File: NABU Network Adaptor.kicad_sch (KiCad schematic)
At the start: 20 parts, among them J2 PC, J3 RF Module, J5 LEDs, U1 SN74LS164N, U10 UA9638CP, U11 UA9637ATC, U13 SN74LS164N, U19 LM339N, U20 SN74LS164N, U21 SN74LS86N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

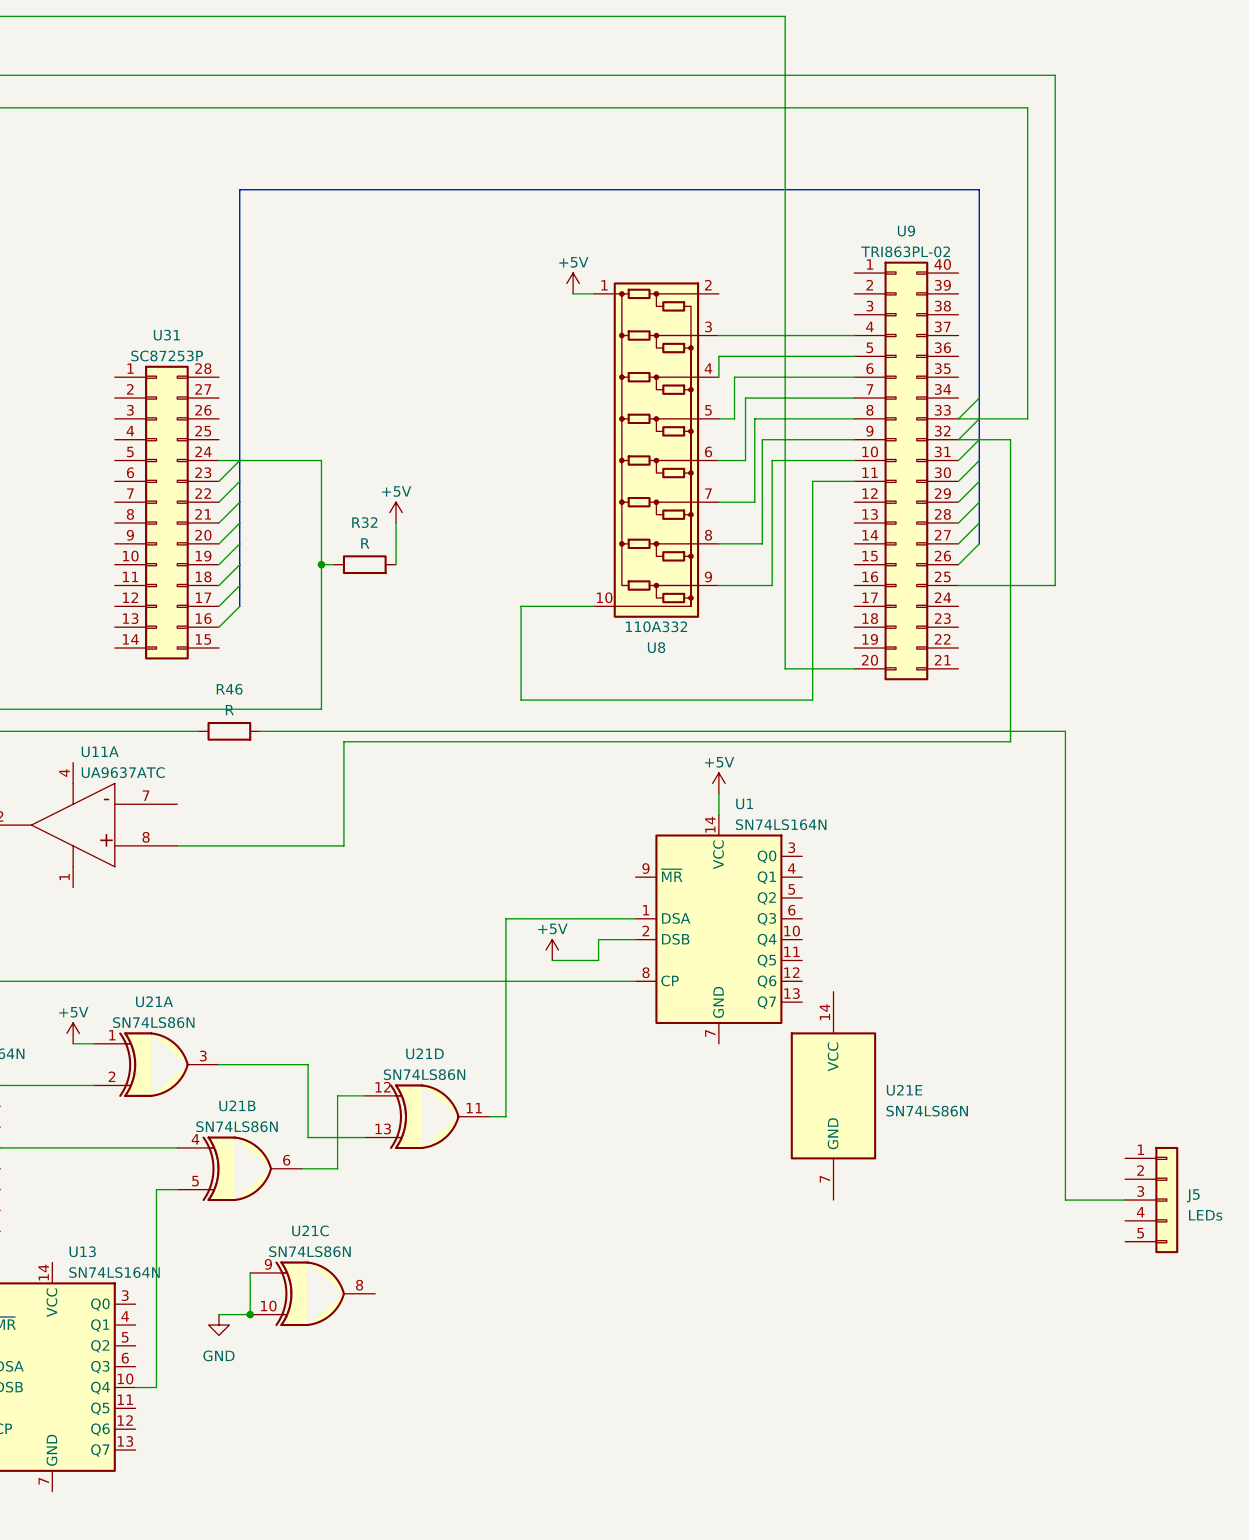
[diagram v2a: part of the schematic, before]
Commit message: Add LED wiring
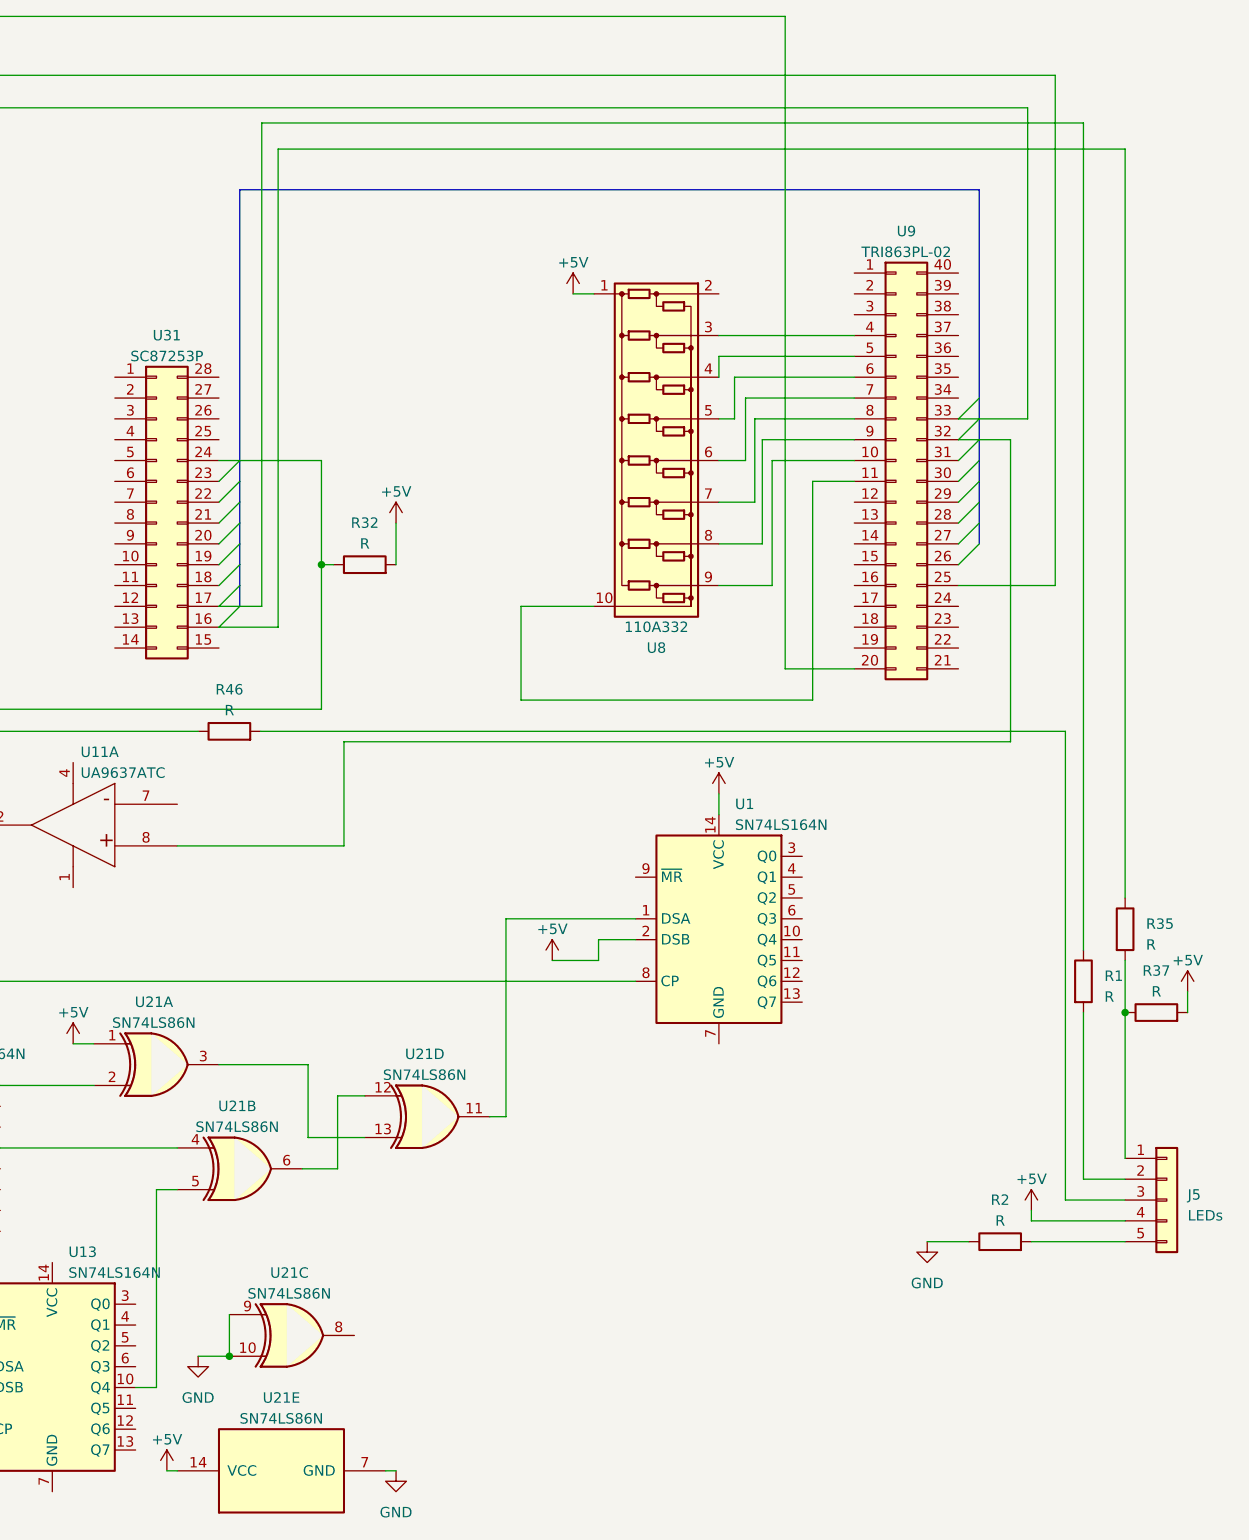
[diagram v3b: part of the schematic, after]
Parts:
- added R1, R2, R35, R37: R, symbol Device:R
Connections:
- net +5V: now also J5.4 (Pin_4), U21.14 (VCC), R37.2
- net GND: now also U21.7 (GND), R2.1
- net at J5.1 (Pin_1): now also R35.2, R37.1
- net at J5.2 (Pin_2): now also R1.2
- net at J5.5 (Pin_5): now also R2.2
- net at U31.16 (Pin_16): now also R35.1
- net at U31.17 (Pin_17): now also R1.1
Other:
- moved on the sheet: U21C, U21E

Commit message: More info on the 74164s
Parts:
- added C1, C12, C13, C20, CB1: C, symbol Device:C
- added U12: SN74LS164N, symbol 74xx:74HCT164
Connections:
- net +5V: now also U13.14 (VCC), U13.2 (DSB), U20.14 (VCC), U20.2 (DSB), C1.2, C12.2, C13.2, C20.2, CB1.1, U12.14 (VCC), U12.2 (DSB)
- net GND: now also U1.7 (GND), U13.7 (GND), C1.1, C12.1, C13.1, C20.1, U12.7 (GND)
- net at R3.2, U20.9 (~{MR}): now also U13.9 (~{MR}), U12.9 (~{MR})
- net at U13.1 (DSA): now also U12.13 (Q7)
- net at U13.8 (CP): now also U1.8 (CP), U20.8 (CP), U23.5 (Q), U24.10, U12.8 (CP)
- net at U1.12 (Q6): now also CB1.2
- net at U20.13 (Q7): now also U12.1 (DSA)
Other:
- moved on the sheet: J2, J3, J5, R1, R2, R3, R32, R35, R37, R38, R43, R46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
